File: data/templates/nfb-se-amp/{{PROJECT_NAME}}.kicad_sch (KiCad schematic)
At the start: 11 parts, among them X1 6P14P, X2 OPT_SE_5K_8

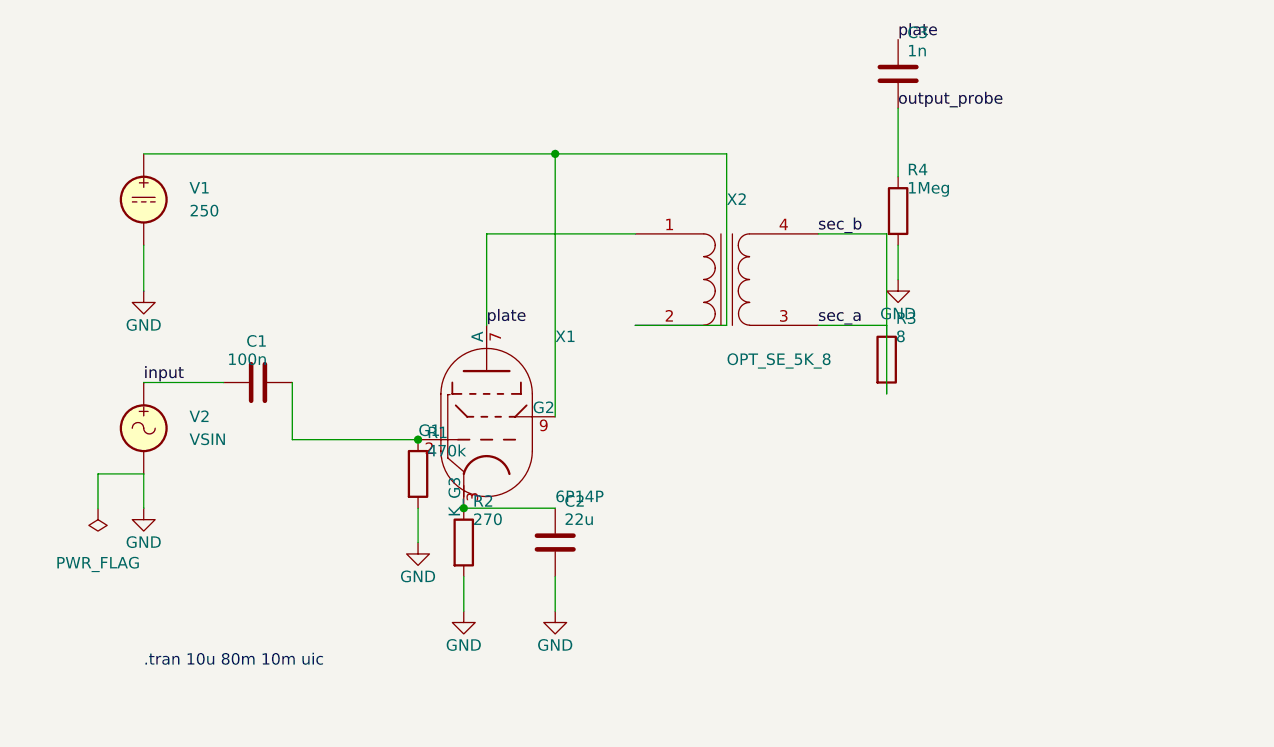
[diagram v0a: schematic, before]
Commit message: T153 Phase B.6: bridge measure phase-margin CLI + slash + KB sync (#94)
* T153: spec Clarified — 4 injection methods + auto-detect + T021 ext

Полнофункциональная реализация (не MVP) после Clarify-раунда:
- Q2=c: все 4 injection methods (Middlebrook V/I, Tian, Rosenstark)
- Q3=b: heuristic auto-detect feedback break node + confirmation
- Q11=a: T021 edit-and-resim расширяется phase-margin метрикой
- Q12=b: Level 3 smoke obligatory как acceptance gate
- Остальные 9 ответов — по рекомендации.

BOARD: BACKLOG → Doing. BACKLOG-запись закомменчена с pointer.

* T153: spec Analyzed — 6 Critical / 8 Warning / 6 Note

Analyze прошёл. 6 Critical (C1 Tian formula verification, C2 op-amp
.subckt, C3 graph placement, C4 confidence convention, C5+C6 NFB
fixture strategy) — половина закрыта inline (C3/C4), остальные —
action items для Phase 0/A. W2 resolved sanity-check'ом (AcSweep
уже pydantic frozen).

* T153 Phase 0: ADR-T153a injection strategy + ADR-T153b graph analyzer

ADR-T153a — 4 loop-gain methodologies (strategy pattern):
- Middlebrook V (1975), Middlebrook I (1975) — single-sweep
- Tian (2001) — symmetric, often equivalent Middlebrook double
- Rosenstark return-ratio (1984) — open/short-circuit topology mod
Terminology correction после Phase 0 research: «Rosenstark double-
injection» (wrong) → «Rosenstark return-ratio»; Tian 1998→2001.
Formula verification — TDD cross-validation в Phase B (IEEE PDFs
за paywall, WebFetch недоступен).

ADR-T153b — NetlistGraphAnalyzer в src/domain/netlist_graph.py:
- Parser → CircuitGraph (nets=vertices, elements=edges)
- DFS cycle detection
- Element-type heuristics: forward path = contains active
  (BJT/MOSFET/E/subckt); feedback = purely passive (R/L/C)
- Break node = high-impedance node на границе forward/feedback
- Confidence = weighted sum, calibrated на N≥3 fixtures в Phase A

* T153 Phase A.1: GENERIC_OPAMP macromodel + opamp ComponentCategory

Cross-validation reference для phase-margin injection methods (Phase B-C):
single-pol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
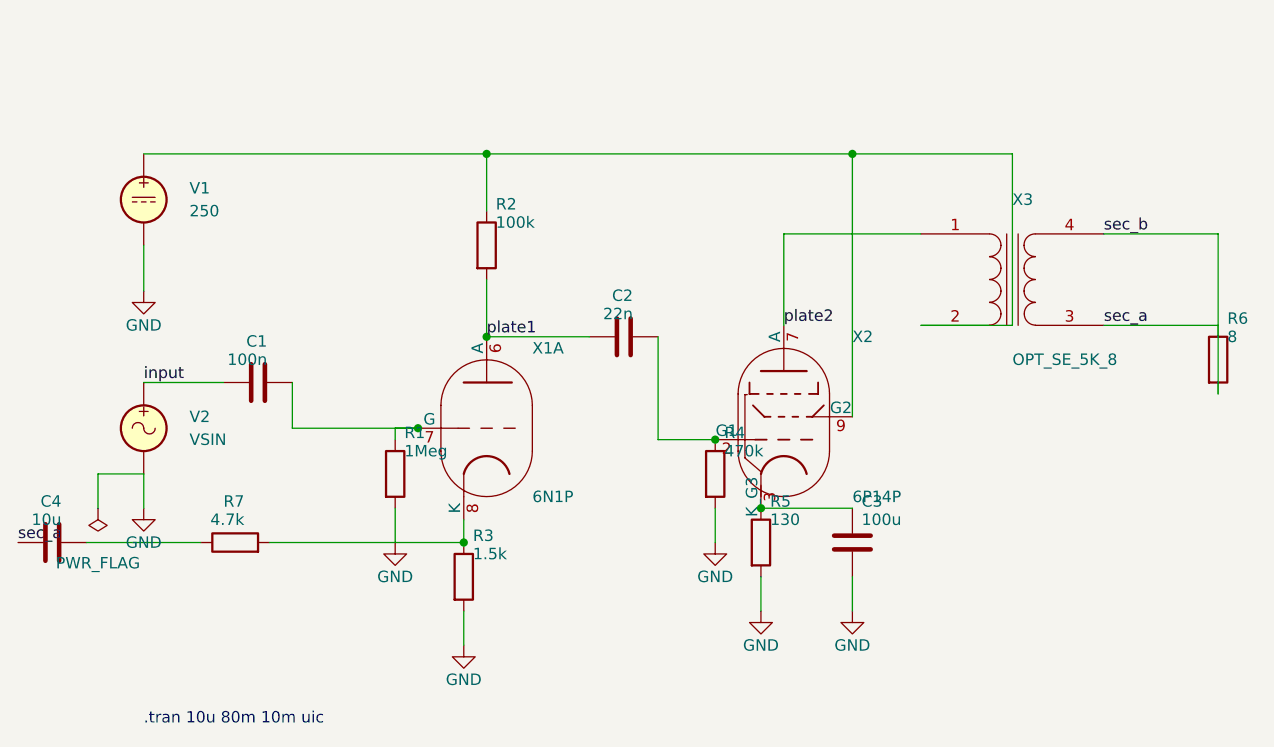
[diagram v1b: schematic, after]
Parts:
- removed X1: 6P14P, symbol Valve:EL84
- removed X2: OPT_SE_5K_8, symbol Device:Transformer_1P_1S
- added C4: 10u, symbol Device:C
- added R5: 130, symbol Device:R
- added R6: 8, symbol Device:R
- added R7: 4.7k, symbol Device:R
- added X1: 6N1P, symbol Valve:ECC81
- added X2: 6P14P, symbol Valve:EL84
- added X3: OPT_SE_5K_8, symbol Device:Transformer_1P_1S
- C2: value 22u -> 22n
- C3: value 1n -> 100u
- R1: value 470k -> 1Meg
- R2: value 270 -> 100k
- R3: value 8 -> 1.5k
- R4: value 1Meg -> 470k
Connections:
- net GND: now also C3.2, R3.2, R5.2; no longer C2.2, R2.2
- net sec_a: now also C4.1, R6.1, X3.3 (SA); no longer R3.1
- net sec_b: now also R6.2, X3.4 (SB); no longer R3.2
- net at R2.1: now also V1.1, X2.9 (G2), X3.2 (AB); no longer C2.1
- net at C1.2, R1.1: now also X1.7 (G)
- net output_probe: no longer names the net of R4.1
- net output_probe: now also C2.2, X2.2 (G1); no longer C3.2
- net plate: no longer names the net of C3.1
- net plate: now also R5.1, X2.3 (K_G3)
- new net: C4.2, R7.1
- new net: R3.1, R7.2, X1.8 (K)
- new net plate1: C2.1, R2.2, X1.6 (A)
- new net plate2: X2.7 (A), X3.1 (AA)
